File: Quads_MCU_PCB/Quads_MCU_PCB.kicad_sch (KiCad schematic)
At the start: 84 parts, among them J1 USB_C_Receptacle_USB2.0_16P, J2 Conn_01x06_Pin, J3 Conn_01x02_Pin, J4 Conn_01x03_Pin, J5 Conn_01x03_Pin, J6 Conn_01x03_Pin, J7 Conn_01x03_Pin, SW1 SW_Push, U1 STM32H723ZGTx, U3 ISOW1044, U4 TSR_1-2450, U5 AP7361C-33E, U6 ISOW1044, U7 ISOW1044, U8 MCP2518FD-xQBB, U9 ISOW1044, Y1 40MHz

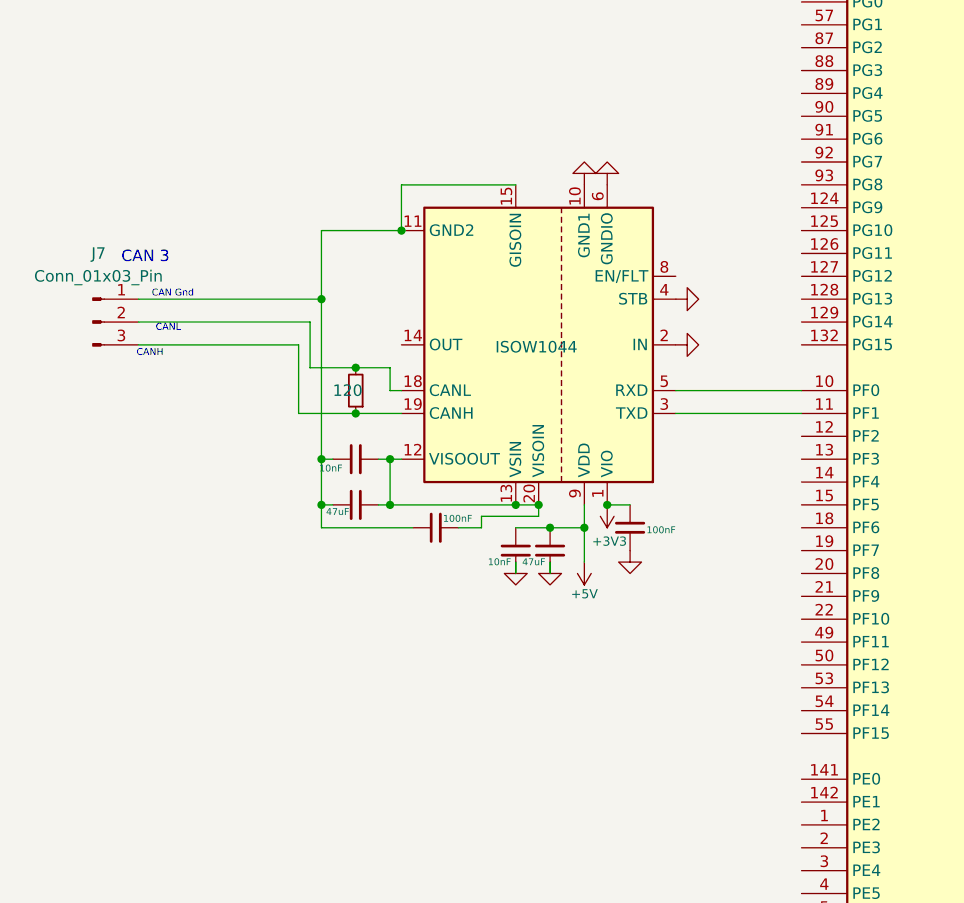
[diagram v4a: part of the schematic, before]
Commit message: Fixed CAN pin connections
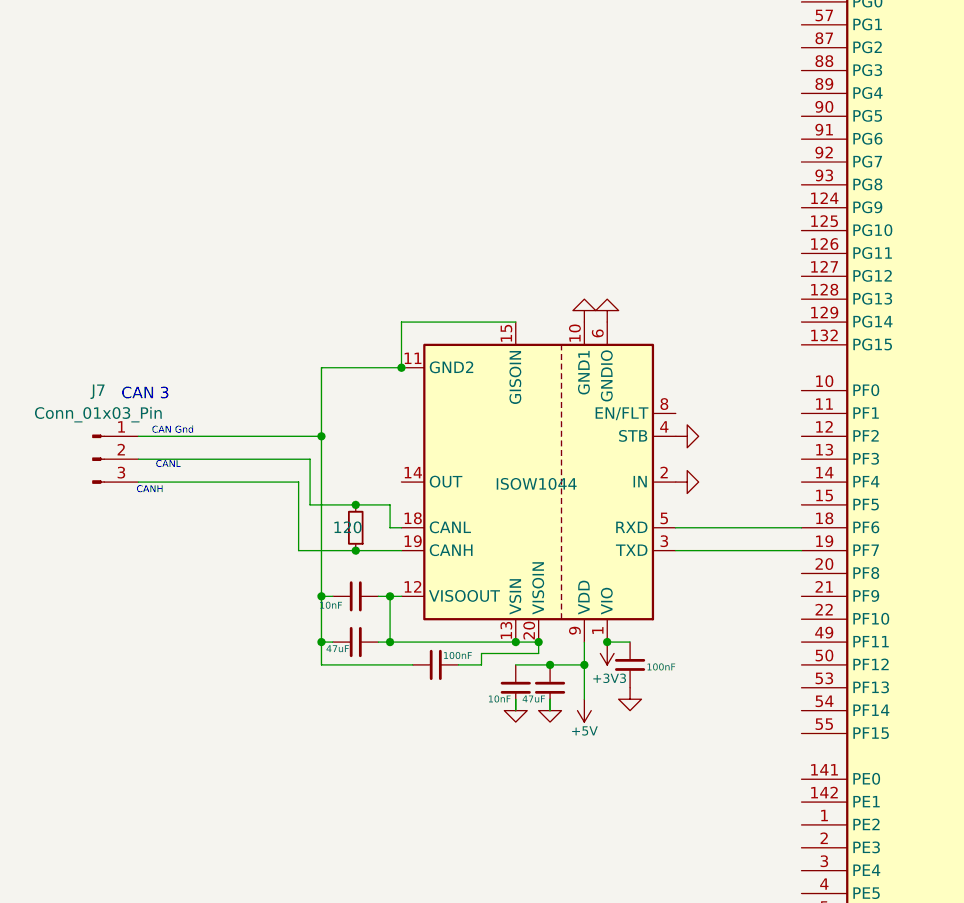
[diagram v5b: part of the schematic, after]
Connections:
- net at U7.3 (TXD): now also U1.19 (PF7); no longer U1.11 (PF1)
- net at U7.5 (RXD): now also U1.18 (PF6); no longer U1.10 (PF0)
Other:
- moved on the sheet: J7

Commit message: Fixed VBUS voltage divider
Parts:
- R4: value 100k -> 4.7k
- R5: value 68k -> 10k

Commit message: Switched to active oscillators and added MCU clock
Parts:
- removed C48: 14pF, symbol Device:C_Small
- removed Y1: 40MHz, symbol Device:Crystal_GND24_Small
- added C58: 100nF, symbol Device:C_Small
- added R7, R8: 22, symbol Device:R_Small
- added Y1: 40MHz, Oscillator:Oscillator_SMD_Abracon_ASE-4Pin_3.2x2.5mm, symbol Oscillator:ASE-xxxMHz
- added Y2: 25MHz, Oscillator:Oscillator_SMD_Abracon_ASE-4Pin_3.2x2.5mm, symbol Oscillator:ASE-xxxMHz
- C57: value 14pF -> 100nF
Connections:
- net +3V3: now also C57.2, C58.2, Y1.1 (EN), Y1.4 (Vdd), Y2.1 (EN), Y2.4 (Vdd)
- net GND: now also C57.1, C58.1, Y1.2 (GND), Y2.2 (GND); no longer C57.2
- net at U1.23 (PH0): now also R8.1
- net at U8.6 (OSC1): now also R7.1; no longer C57.1
- new net: R8.2, Y2.3 (OUT)
- new net: R7.2, Y1.3 (OUT)
- no-connect marks 0 -> 107

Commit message: Fixed ERC tests
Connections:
- no-connect marks 107 -> 110
